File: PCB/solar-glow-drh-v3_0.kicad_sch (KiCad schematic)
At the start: 63 parts, among them J1 UPDI hdr, Q1 BCP5316MTWG, SW2 LED master, U1 AVR64DD28 (VQFN28), U2 ALD910025SALI, U3 ADXL367, U4 TLV3011BIDBVR, U5 NT3H2211, U6 TPS22918

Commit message: sch: enrich component fields (datasheet, MPN, description) from the BOM
All 63 components: Datasheet -> renamed file, new MPN field, filled Description. ERC 0 errors and the pin-map consistency check still passes -- metadata only, connectivity untouched.

Co-Authored-By: Claude Opus 4.8 <noreply@anthropic.com>
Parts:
- C1, C10, C12, C2, C3, C6, C7, C8: MPN (none) -> GRM155R71C104KA88D
- C11: MPN (none) -> GRM155 0.22uF (verify MPN)
- C13: MPN (none) -> GRM155R61A475ME15D
- C4: MPN (none) -> GRM155R61A105KE15D
- C5: MPN (none) -> GRM155R71C103KA01D
- C9: MPN (none) -> (DNP)
- D1, D10, D11, D9: MPN (none) -> MMSD301T1G
- D2, D3, D4, D5: MPN (none) -> LA P47F-V2BB-24-3B5A-30-R18-Z
- J1: MPN (none) -> (unpopulated header)
- JP1: MPN (none) -> (bare pads - no part)
- L1: MPN (none) -> (PCB feature - no part)
- MH1, MH2, MH3, MH4: MPN (none) -> (drill - no part)
- PV1, PV2: MPN (none) -> SM141K06TF
- Q1: MPN (none) -> BCP5316MTWG
- R1, R2, R3, R4: MPN (none) -> RC0402FR-07150RL
- R10, R11: MPN (none) -> RC0402FR-074K7L
- R12: MPN (none) -> RC0402FR-07220RL
- R13: MPN (none) -> RC0402FR-0710KL
- R14: MPN (none) -> RC0402FR-07100KL
- R5, R6: MPN (none) -> RC0402FR-071ML
- R7: MPN (none) -> RC0402FR-076M81L
- R8: MPN (none) -> RC0402FR-073M74L
- R9: MPN (none) -> RC0402FR-071KL
- SB1, SB2, SB3, SB4, SW2: MPN (none) -> (PCB bridge - no part)
- SC1, SC2, SC3, SC4: MPN (none) -> 3-153-438
- SJ1: MPN (none) -> RC0805JR-070RL
- TC1: MPN (none) -> (no part - pogo footprint)
- TP1: MPN (none) -> (bare pad - no part)
- U1: MPN (none) -> AVR64DD28-I/STX
- U2: MPN (none) -> ALD910025SALI
- U3: MPN (none) -> ADXL367BCCZ-RL7
- U4: MPN (none) -> TLV3011BIDBVR
- U5: MPN (none) -> NT3H2211W0FHKH
- U6: MPN (none) -> TPS22918DBVR

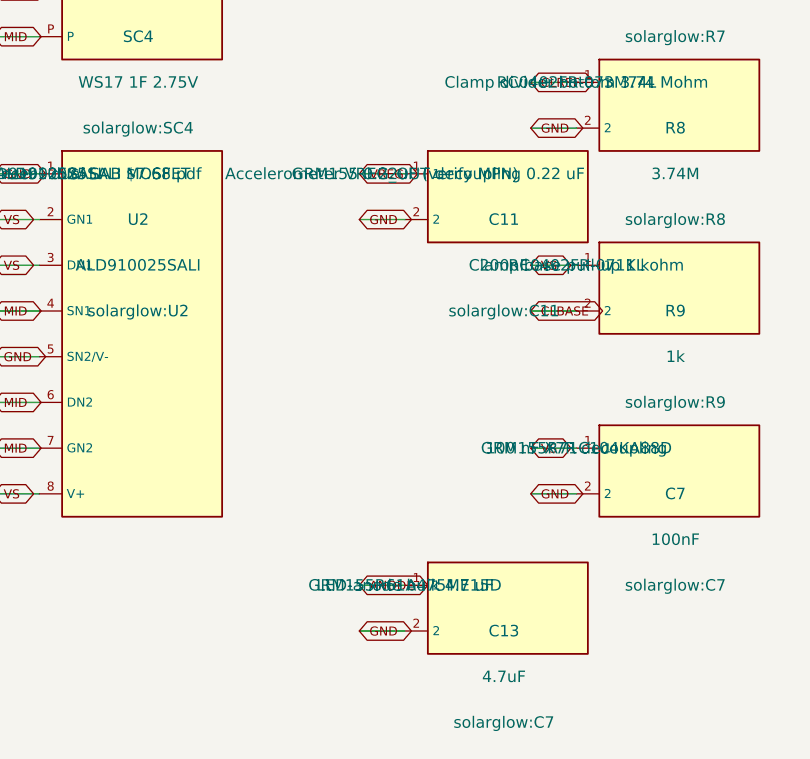
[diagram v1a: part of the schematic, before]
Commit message: bom, sch: correct 4 items from PCBWay assembly review (T-H70W567099A)
R7 Manufacturer had a stray old part number (RC0402FR-071M82L) instead of Yageo. D2-D5 package corrected to SMD 3.4x1.9 mm. C11 MPN -> GRM155R71C224KA12D (0.22uF 16V X7R 0402). C13 MPN -> GRM155R61A475MEAAD (4.7uF 10V X5R 0402). Both cap MPNs DigiKey-verified in stock. Applied to both BOM .xlsx and the schematic; ERC 0, consistency passes.

Co-Authored-By: Claude Opus 4.8 <noreply@anthropic.com>
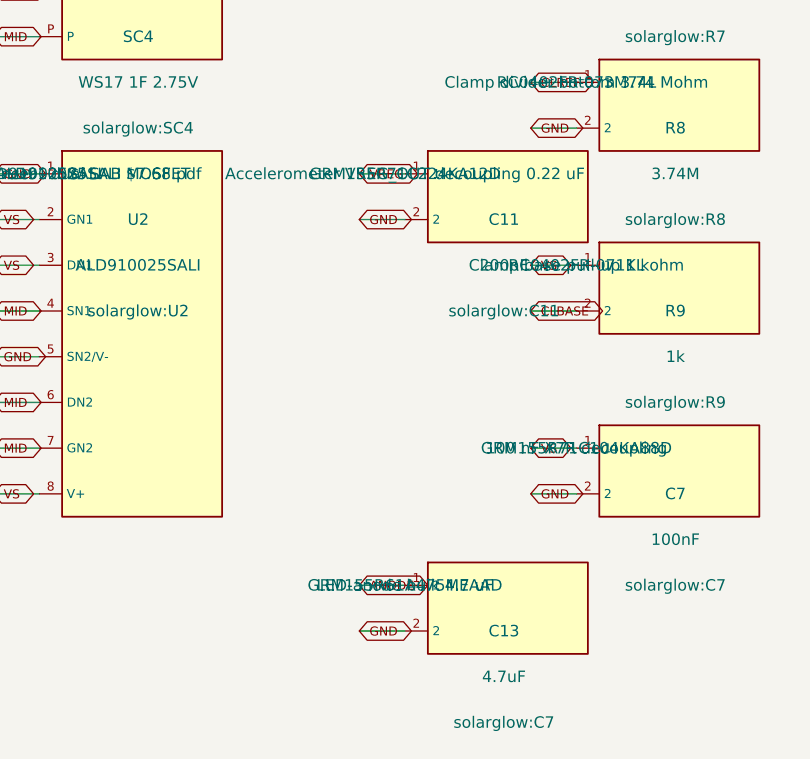
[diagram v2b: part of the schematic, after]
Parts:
- C11: MPN GRM155 0.22uF (verify MPN) -> GRM155R71C224KA12D
- C13: MPN GRM155R61A475ME15D -> GRM155R61A475MEAAD

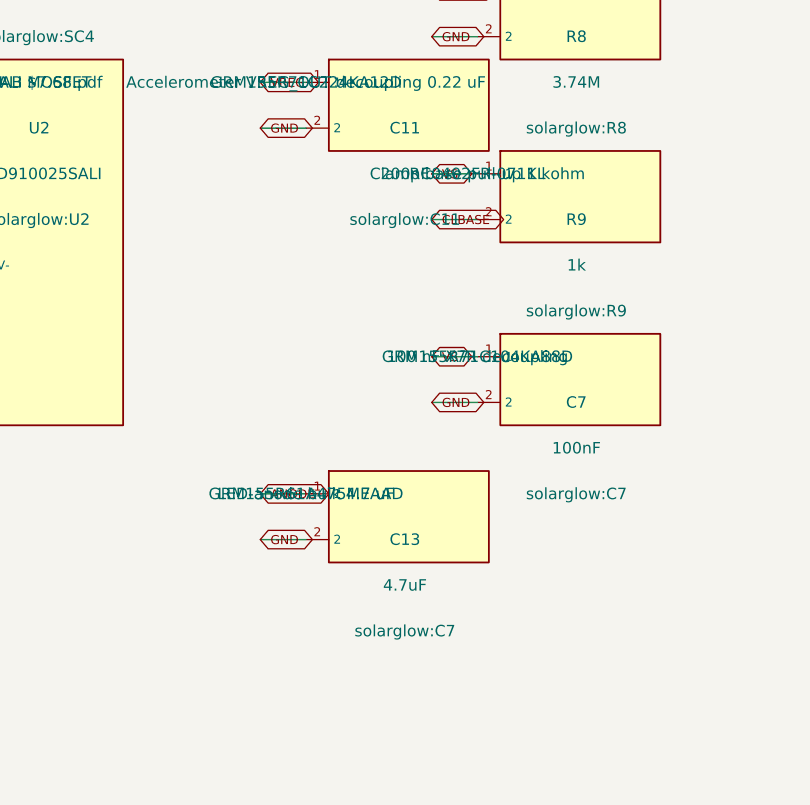
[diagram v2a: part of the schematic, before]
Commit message: PCB: fix C13 footprint id (solarglow:C7 -> C13) and C11 value (200nF -> 220nF)
Two board-file corrections from the PCB audit. Identifier/value strings only,
no copper/pad/geometry change. Verified by exact single-token git diff, real-C7
untouched (pcb 7364, sch 3147), and unchanged paren balance in both files.

C13 footprint id: the footprint carried the stale base-footprint string
"solarglow:C7" in both the .kicad_pcb block (uuid 355e5d4a) and the .kicad_sch
Footprint property, a leftover from when C13 was split off C7. Caps are named
per refdes (solarglow:C1..C12); there was no solarglow:C13 and a duplicated
solarglow:C7. Renamed C13's footprint id to solarglow:C13 in both files. Also
clears the CI BOM's bogus Footprint=C7 column for C13.

C11 value: MPN GRM155R71C224KA12D is 0.22 uF (220 nF) but the value field read
"200nF". Corrected the instance and the lib-symbol default to "220nF".

Not changed (audit conclusions): L1 was already 1.0uH; R5/R6 "VSENSE div" and
the other descriptive value labels are house style, not placeholders (the BOM
grouping fix is a KiBot group-by-MPN config change, handed off separately); the
origin NPTH_mech footprint carries real non-plated holes and is not a stray.

Co-Authored-By: Claude Opus 4.8 <noreply@anthropic.com>
Claude-Session: https://claude.ai/code/session_01PBK3zFENdvoGtn8yP7qPA8
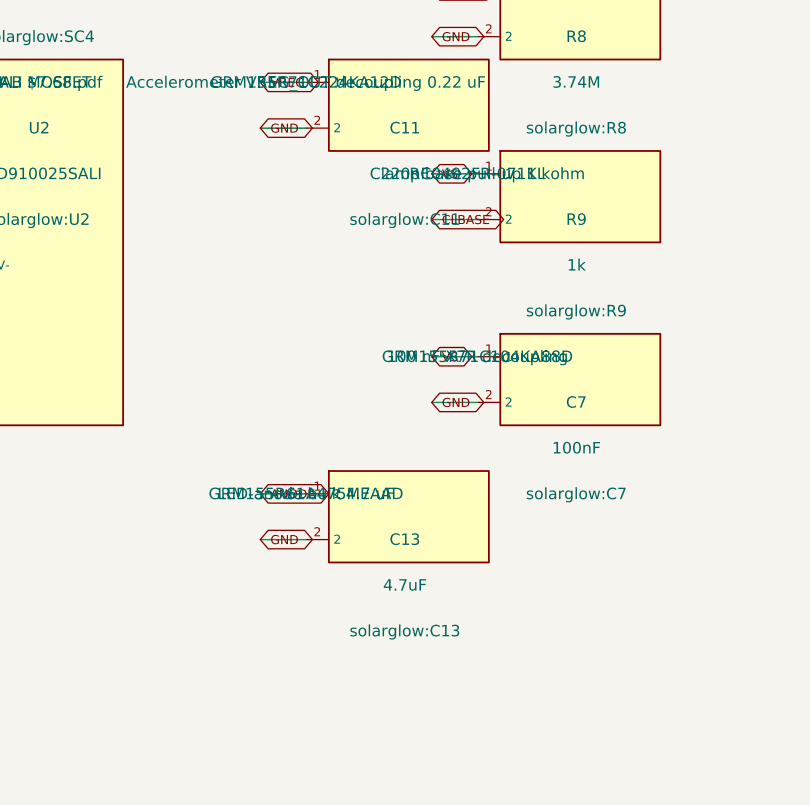
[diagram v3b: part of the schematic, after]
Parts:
- C11: value 200nF -> 220nF
- C13: footprint solarglow:C7 -> solarglow:C13
